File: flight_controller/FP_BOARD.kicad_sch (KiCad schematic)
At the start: 4 parts

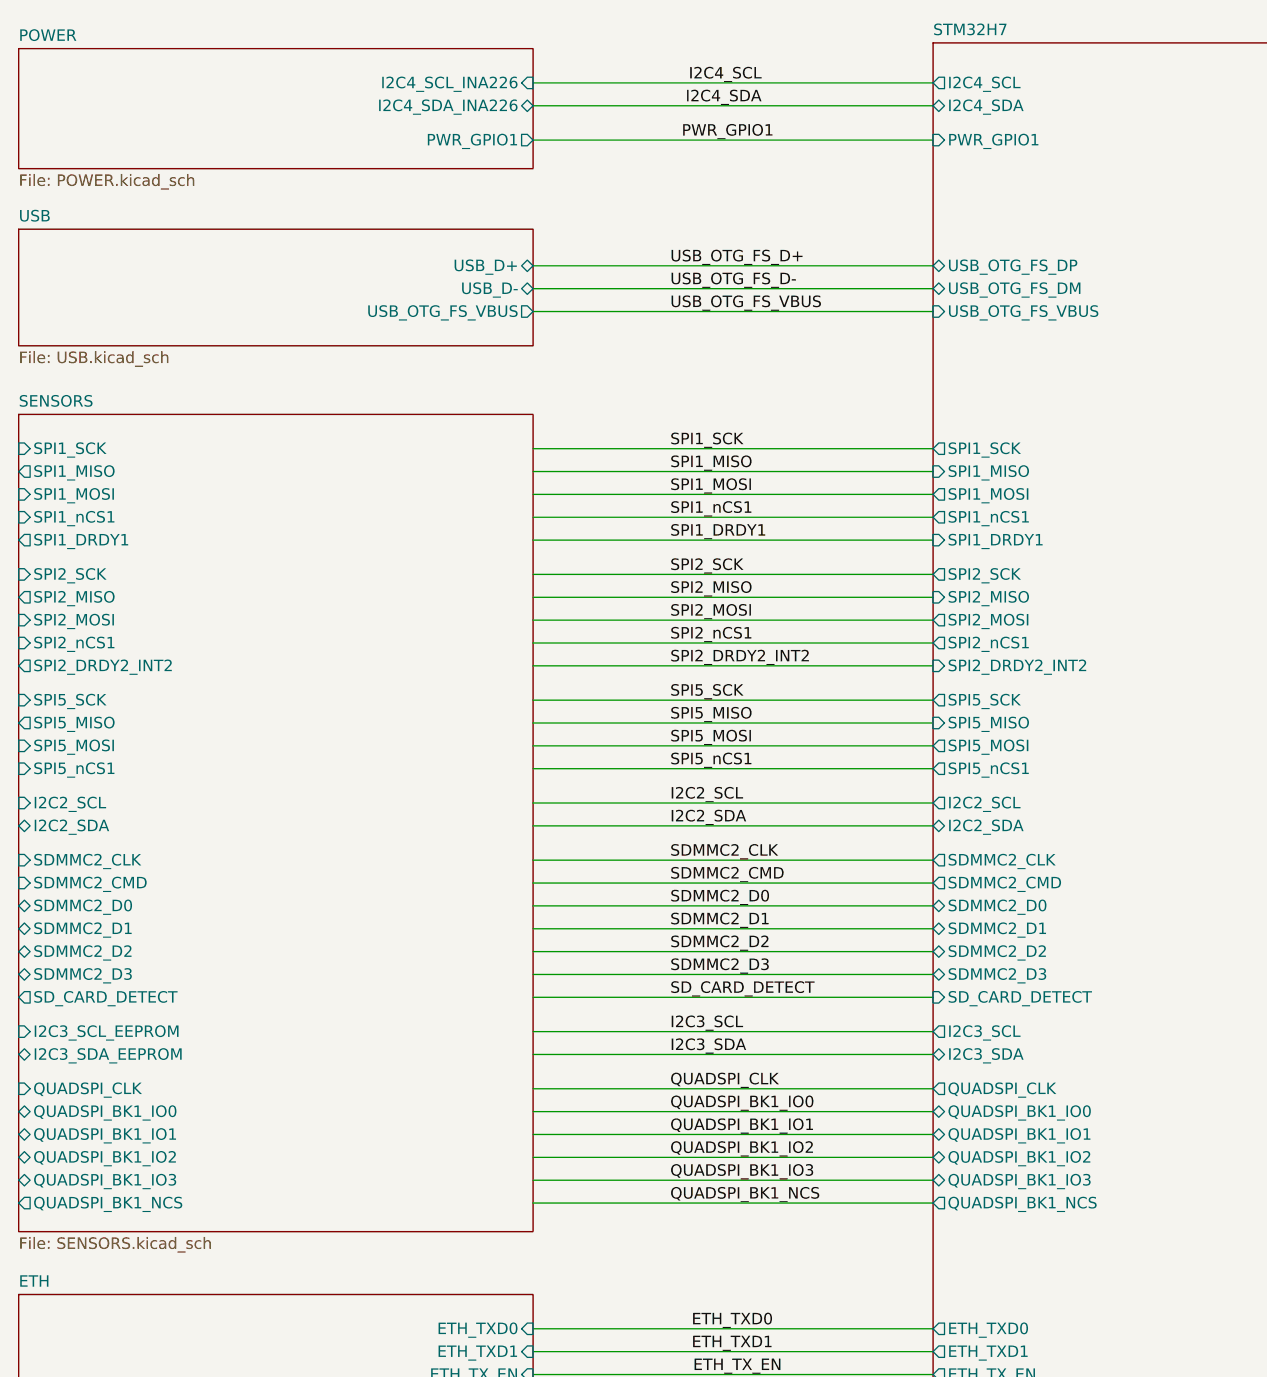
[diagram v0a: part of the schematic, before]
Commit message: Updated power and usb connectors and netlist check
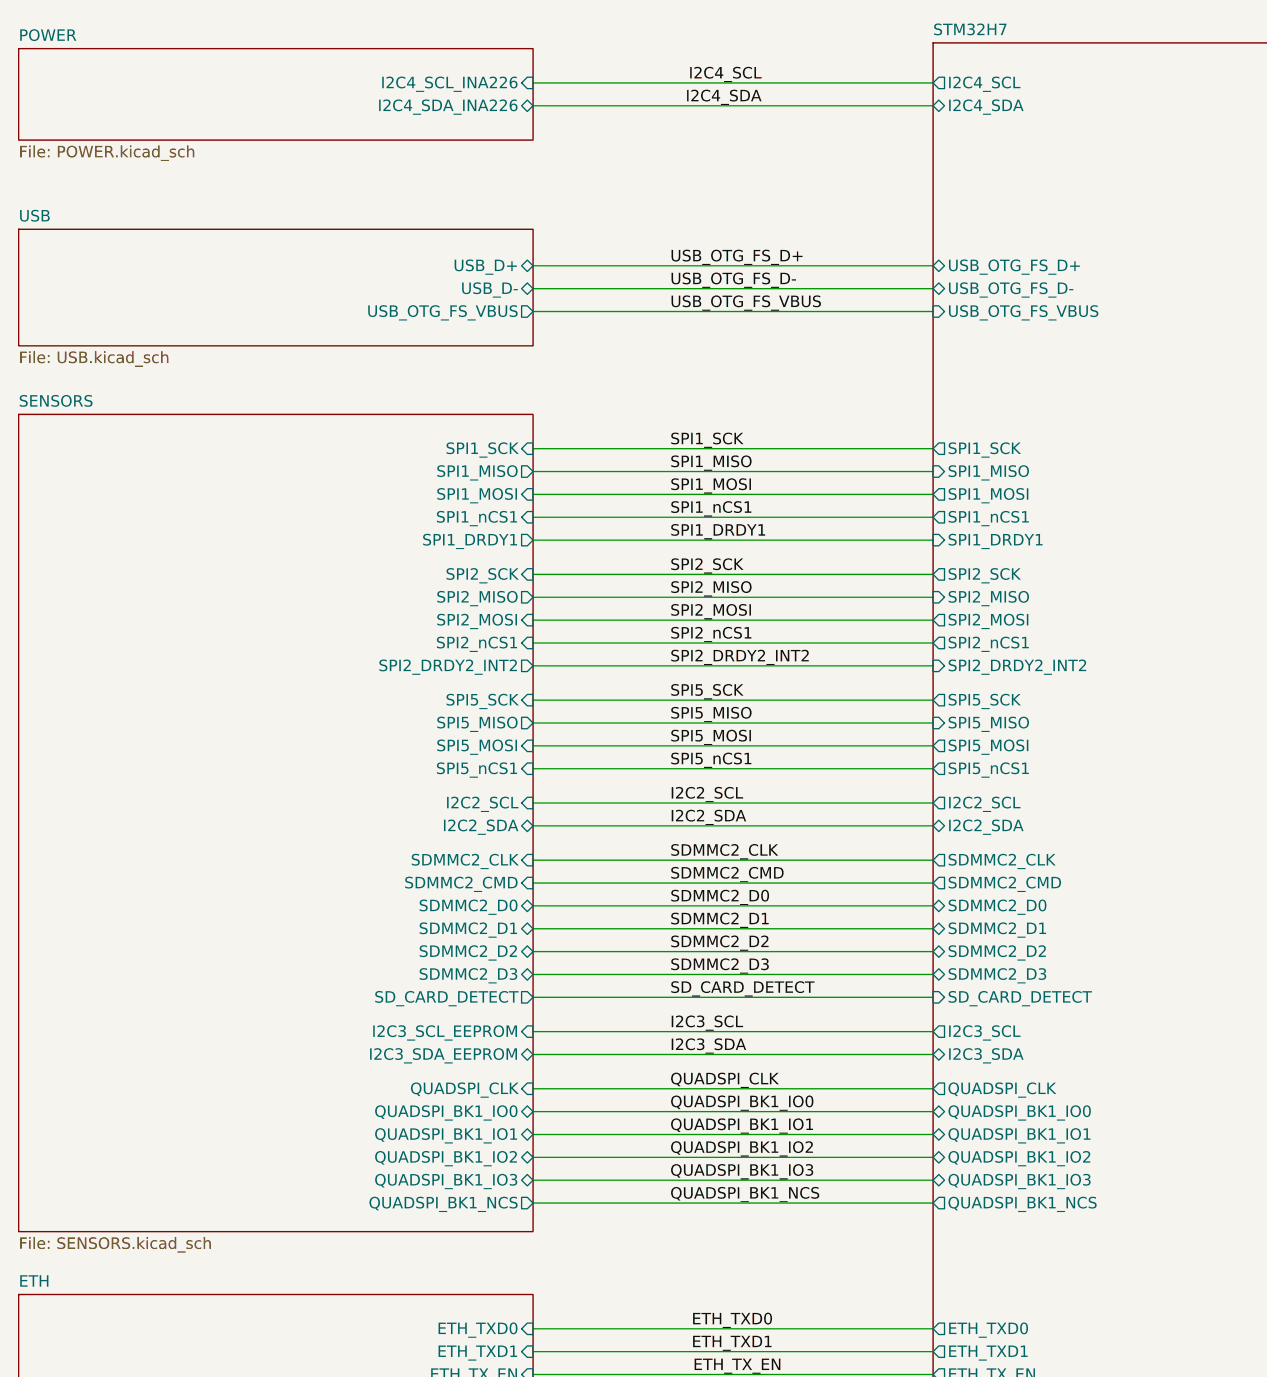
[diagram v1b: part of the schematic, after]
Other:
- sheet POWER ports: added none; removed PWR_GPIO1
- sheet STM32H7 ports: added USB_OTG_FS_D+, USB_OTG_FS_D-; removed PWR_GPIO1, USB_OTG_FS_DM, USB_OTG_FS_DP
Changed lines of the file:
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@@
 	(wire
 		(pts
-			(xy 209.55 68.58) (xy 254 68.58)
-		)
-		(stroke
-			(width 0)
-			(type default)
-		)
-	)
-	(wire
-		(pts
 			(xy 330.2 81.28) (xy 431.8 81.28)
 		)
@@
 		)
 	)
-	(label "PWR_GPIO1"
-		(at 226.06 68.58 0)
-		(effects
-			(font
-				(size 1.27 1.27)
-			)
-			(justify left bottom)
-		)
-	)
 	(label "SD_CARD_DETECT"
 		(at 224.79 163.83 0)
@@
 	(sheet
 		(at 152.4 58.42)
-		(size 57.15 13.335)
+		(size 57.15 10.16)
 		(exclude_from_sim no)
 		(in_bom yes)
@@
 		)
 		(property "Sheetfile" "POWER.kicad_sch"
-			(at 152.4 72.3396 0)
+			(at 152.4 69.1646 0)
 			(effects
 				(font
@@
 			)
 		)
-		(pin "PWR_GPIO1" output
-			(at 209.55 68.58 0)
-			(effects
-				(font
-					(size 1.27 1.27)
-				)
-				(justify right)
-			)
-		)
 		(instances
 			(project "FP_BOARD"
@@
 			)
 		)
-		(pin "PWR_GPIO1" input
-			(at 254 68.58 180)
-			(effects
-				(font
-					(size 1.27 1.27)
-				)
-				(justify left)
-			)
-		)
 		(pin "USB_OTG_FS_VBUS" input
 			(at 254 87.63 180)
@@
 			)
 		)
-		(pin "USB_OTG_FS_DM" bidirectional
-			(at 254 85.09 180)
+		(pin "USB_OTG_FS_D+" bidirectional
+			(at 254 82.55 180)
 			(effects
 				(font
@@
 			)
 		)
-		(pin "USB_OTG_FS_DP" bidirectional
-			(at 254 82.55 180)
+		(pin "USB_OTG_FS_D-" bidirectional
+			(at 254 85.09 180)
 			(effects
 				(font
@@
 		)
 		(pin "I2C2_SCL" input
-			(at 152.4 142.24 180)
+			(at 209.55 142.24 0)
 			(effects
 				(font
 					(size 1.27 1.27)
 				)
-				(justify left)
+				(justify right)
 			)
 		)
 		(pin "I2C2_SDA" bidirectional
-			(at 152.4 144.78 180)
+			(at 209.55 144.78 0)
 			(effects
 				(font
 					(size 1.27 1.27)
 				)
-				(justify left)
+				(justify right)
 			)
 		)
 		(pin "SDMMC2_CLK" input
-			(at 152.4 148.59 180)
+			(at 209.55 148.59 0)
 			(effects
 				(font
 					(size 1.27 1.27)
 				)
-				(justify left)
+				(justify right)
 			)
 		)
 		(pin "SDMMC2_CMD" input
-			(at 152.4 151.13 180)
+			(at 209.55 151.13 0)
 			(effects
 				(font
 					(size 1.27 1.27)
 				)
-				(justify left)
+				(justify right)
 			)
 		)
 		(pin "SDMMC2_D0" bidirectional
-			(at 152.4 153.67 180)
+			(at 209.55 153.67 0)
 			(effects
 				(font
 					(size 1.27 1.27)
 				)
-				(justify left)
+				(justify right)
 			)
 		)
 		(pin "SDMMC2_D1" bidirectional
-			(at 152.4 156.21 180)
+			(at 209.55 156.21 0)
 			(effects
 				(font
 					(size 1.27 1.27)
 				)
-				(justify left)
+				(justify right)
 			)
 		)
 		(pin "SDMMC2_D2" bidirectional
-			(at 152.4 158.75 180)
+			(at 209.55 158.75 0)
 			(effects
 				(font
 					(size 1.27 1.27)
 				)
-				(justify left)
+				(justify right)
 			)
 		)
 		(pin "SDMMC2_D3" bidirectional
-			(at 152.4 161.29 180)
+			(at 209.55 161.29 0)
 			(effects
 				(font
 					(size 1.27 1.27)
 				)
-				(justify left)
+				(justify right)
 			)
 		)
 		(pin "SPI1_DRDY1" output
-			(at 152.4 113.03 180)
+			(at 209.55 113.03 0)
 			(effects
 				(font
 					(size 1.27 1.27)
 				)
-				(justify left)
+				(justify right)
 			)
 		)
 		(pin "SPI1_MISO" output
-			(at 152.4 105.41 180)
+			(at 209.55 105.41 0)
 			(effects
 				(font
 					(size 1.27 1.27)
 				)
-				(justify left)
+				(justify right)
 			)
 		)
 		(pin "SPI1_MOSI" input
-			(at 152.4 107.95 180)
+			(at 209.55 107.95 0)
 			(effects
 				(font
 					(size 1.27 1.27)
 				)
-				(justify left)
+				(justify right)
 			)
 		)
 		(pin "SPI1_nCS1" input
-			(at 152.4 110.49 180)
+			(at 209.55 110.49 0)
 			(effects
 				(font
 					(size 1.27 1.27)
 				)
-				(justify left)
+				(justify right)
 			)
 		)
 		(pin "SPI1_SCK" input
-			(at 152.4 102.87 180)
+			(at 209.55 102.87 0)
 			(effects
 				(font
 					(size 1.27 1.27)
 				)
-				(justify left)
+				(justify right)
 			)
 		)
 		(pin "SPI2_DRDY2_INT2" output
-			(at 152.4 127 180)
+			(at 209.55 127 0)
 			(effects
 				(font
 					(size 1.27 1.27)
 				)
-				(justify left)
+				(justify right)
 			)
 		)
 		(pin "SPI2_MISO" output
-			(at 152.4 119.38 180)
+			(at 209.55 119.38 0)
 			(effects
 				(font
 					(size 1.27 1.27)
 				)
-				(justify left)
+				(justify right)
 			)
 		)
 		(pin "SPI2_MOSI" input
-			(at 152.4 121.92 180)
+			(at 209.55 121.92 0)
 			(effects
 				(font
 					(size 1.27 1.27)
 				)
-				(justify left)
+				(justify right)
 			)
 		)
 		(pin "SPI2_nCS1" input
-			(at 152.4 124.46 180)
+			(at 209.55 124.46 0)
 			(effects
 				(font
 					(size 1.27 1.27)
 				)
-				(justify left)
+				(justify right)
 			)
 		)
 		(pin "SPI2_SCK" input
-			(at 152.4 116.84 180)
+			(at 209.55 116.84 0)
 			(effects
 				(font
 					(size 1.27 1.27)
 				)
-				(justify left)
+				(justify right)
 			)
 		)
 		(pin "SPI5_MISO" output
-			(at 152.4 133.35 180)
+			(at 209.55 133.35 0)
 			(effects
 				(font
 					(size 1.27 1.27)
 				)
-				(justify left)
+				(justify right)
 			)
 		)
 		(pin "SPI5_MOSI" input
-			(at 152.4 135.89 180)
+			(at 209.55 135.89 0)
 			(effects
 				(font
 					(size 1.27 1.27)
 				)
-				(justify left)
+				(justify right)
 			)
 		)
 		(pin "SPI5_nCS1" input
-			(at 152.4 138.43 180)
+			(at 209.55 138.43 0)
 			(effects
 				(font
 					(size 1.27 1.27)
 				)
-				(justify left)
+				(justify right)
 			)
 		)
 		(pin "SPI5_SCK" input
-			(at 152.4 130.81 180)
+			(at 209.55 130.81 0)
 			(effects
 				(font
 					(size 1.27 1.27)
 				)
-				(justify left)
+				(justify right)
 			)
 		)
 		(pin "I2C3_SCL_EEPROM" input
-			(at 152.4 167.64 180)
+			(at 209.55 167.64 0)
 			(effects
 				(font
 					(size 1.27 1.27)
 				)
-				(justify left)
+				(justify right)
 			)
 		)
 		(pin "I2C3_SDA_EEPROM" bidirectional
-			(at 152.4 170.18 180)
+			(at 209.55 170.18 0)
 			(effects
 				(font
 					(size 1.27 1.27)
 				)
-				(justify left)
+				(justify right)
 			)
 		)
 		(pin "QUADSPI_BK1_IO0" bidirectional
-			(at 152.4 176.53 180)
+			(at 209.55 176.53 0)
 			(effects
 				(font
 					(size 1.27 1.27)
 				)
-				(justify left)
+				(justify right)
 			)
 		)
 		(pin "QUADSPI_BK1_IO1" bidirectional
-			(at 152.4 179.07 180)
+			(at 209.55 179.07 0)
 			(effects
 				(font
 					(size 1.27 1.27)
 				)
-				(justify left)
+				(justify right)
 			)
 		)
 		(pin "QUADSPI_BK1_IO2" bidirectional
-			(at 152.4 181.61 180)
+			(at 209.55 181.61 0)
 			(effects
 				(font
 					(size 1.27 1.27)
 				)
-				(justify left)
+				(justify right)
 			)
 		)
 		(pin "QUADSPI_BK1_IO3" bidirectional
-			(at 152.4 184.15 180)
+			(at 209.55 184.15 0)
 			(effects
 				(font
 					(size 1.27 1.27)
 				)
-				(justify left)
+				(justify right)
 			)
 		)
 		(pin "QUADSPI_BK1_NCS" output
-			(at 152.4 186.69 180)
+			(at 209.55 186.69 0)
 			(effects
 				(font
 					(size 1.27 1.27)
 				)
-				(justify left)
+				(justify right)
 			)
 		)
 		(pin "QUADSPI_CLK" input
-			(at 152.4 173.99 180)
+			(at 209.55 173.99 0)
 			(effects
 				(font
 					(size 1.27 1.27)
 				)
-				(justify left)
+				(justify right)
 			)
 		)
 		(pin "SD_CARD_DETECT" output
-			(at 152.4 163.83 180)
+			(at 209.55 163.83 0)
 			(effects
 				(font
 					(size 1.27 1.27)
 				)
-				(justify left)
+				(justify right)
 			)
 		)
